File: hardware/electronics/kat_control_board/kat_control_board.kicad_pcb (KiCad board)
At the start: 4 copper layers, 84.2 x 173.5 mm, 122 parts, among them J1 USB_C_Receptacle_USB2.0, J10 Conn_01x04, J11 Conn_01x04, J12 Conn_01x04, J13 Conn_01x04, J14 Conn_01x04, J15 Conn_01x04, J16 Conn_01x04, J17 Conn_01x02, J18 Conn_01x04, J19 Conn_01x04, J2 Conn_01x04, J20 Conn_01x02, J21 Conn_01x02, J22 Conn_01x02, J23 Conn_01x02, J24 Conn_01x02, J25 Conn_01x02, J26 Conn_01x02, J27 Conn_01x02, J28 Conn_01x04, J29 Conn_02x30_Odd_Even, J3 Conn_01x04, J30 Conn_02x30_Odd_Even, J31 Conn_02x30_Odd_Even, J32 Conn_02x30_Odd_Even, J4 Conn_01x04, J5 Conn_01x04, J6 Conn_01x04, J7 Conn_01x04, J8 Conn_01x04, J9 Conn_01x04, Q1 AO3400A, Q2 AO3400A, Q3 AO3400A, Q4 AO3400A, Q5 AO3400A, SW1 SW_SPST, SW2 SW_SPST, U1 RP2040, U2 W25Q128JVS, U3 SN74HC4851, U4 74HCT244, U5 74HCT244, U6 SIC431, U7 XC6206PxxxMR, Y1 12MHz

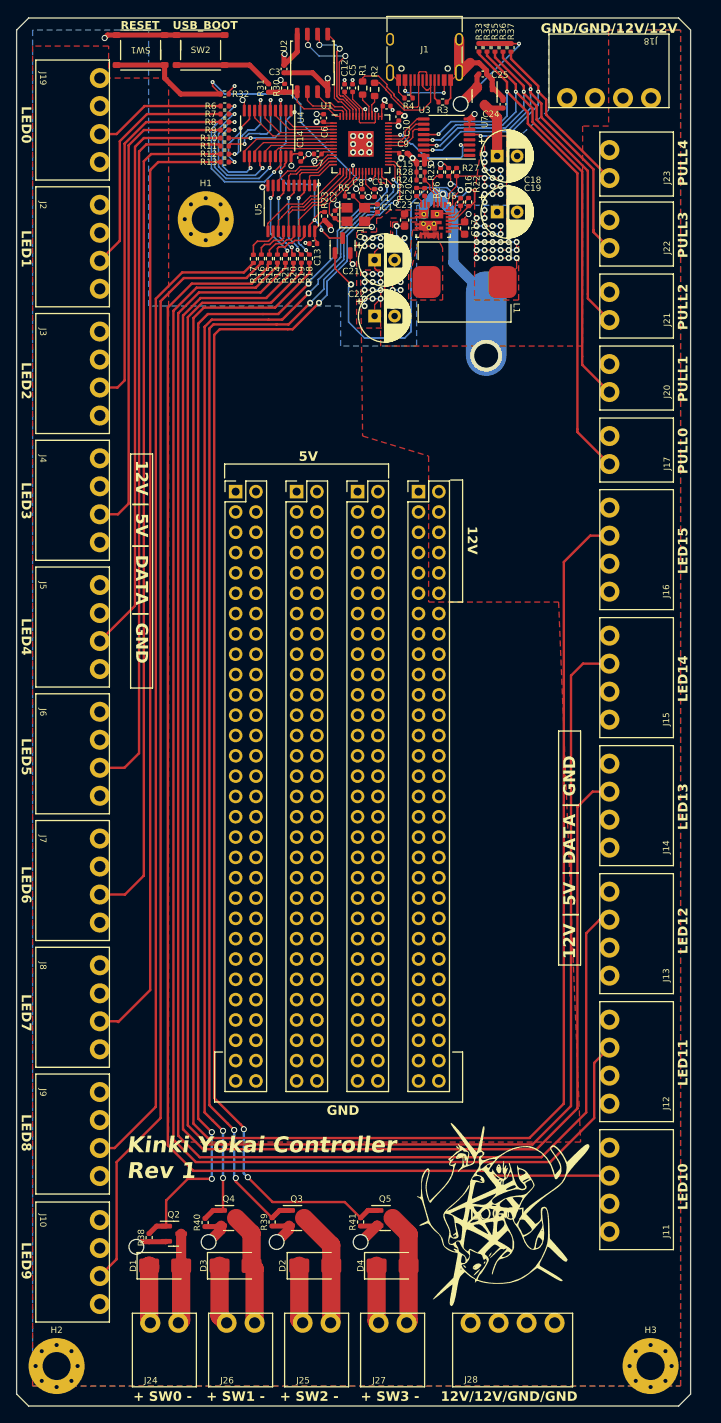
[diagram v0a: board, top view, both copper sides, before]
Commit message: Updated PCB design with more protections
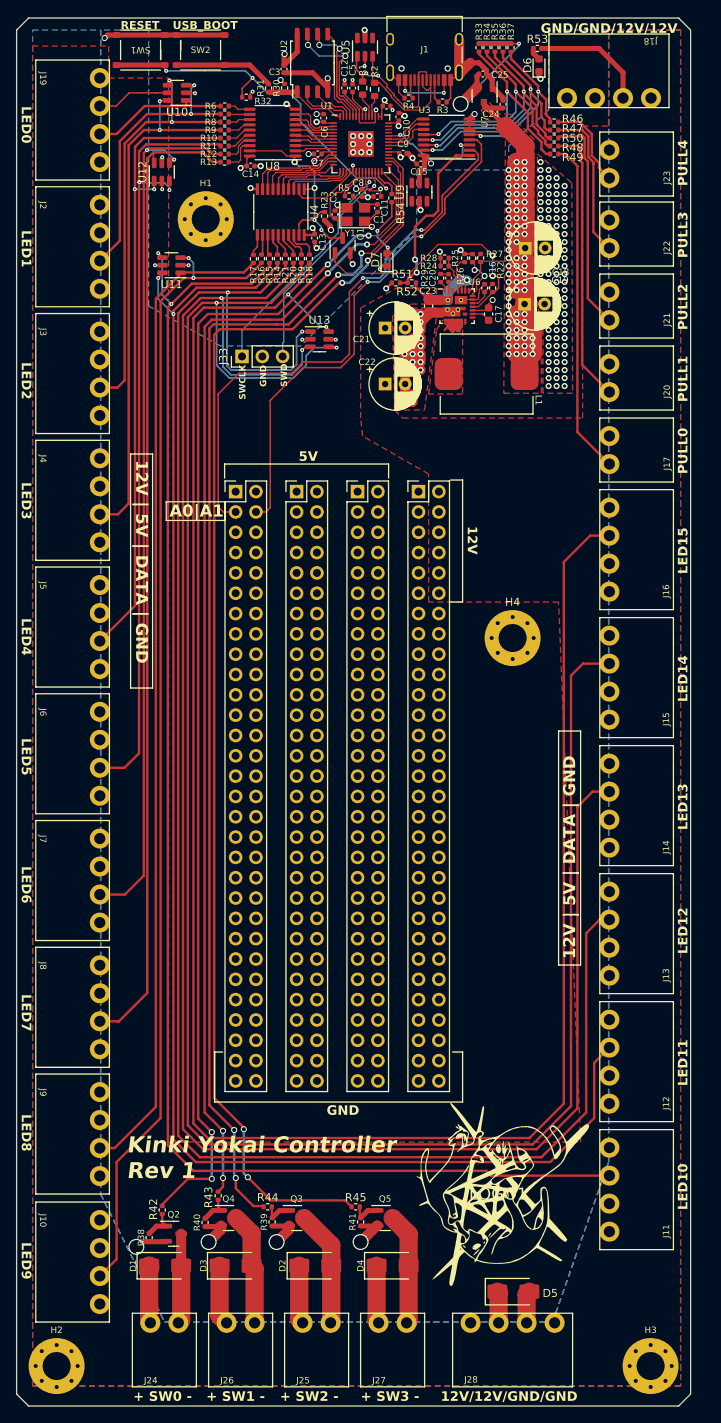
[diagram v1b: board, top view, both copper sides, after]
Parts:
- added D5: M7, Diode_SMD:D_SMA, F.Cu at (90.6, 176.2)
- added D6: RED, LED_SMD:LED_0603_1608Metric, F.Cu at (93.8, 22.9)
- added D7: YELLOW, LED_SMD:LED_0603_1608Metric, F.Cu at (74.8, 47.2)
- added H4: MountingHole, MountingHole:MountingHole_3.5mm_Pad_Via, F.Cu at (90.5, 94.5)
- added J33: Conn_01x03, Connector_PinHeader_2.54mm:PinHeader_1x03_P2.54mm_Vertical, F.Cu at (56.7, 59.3)
- added R42: 100R, Resistor_SMD:R_0402_1005Metric, F.Cu at (46.7, 166.0)
- added R43: 100R, Resistor_SMD:R_0402_1005Metric, F.Cu at (53.7, 164.2)
- added R44: 100R, Resistor_SMD:R_0402_1005Metric, F.Cu at (59.9, 165.6)
- added R45: 100R, Resistor_SMD:R_0402_1005Metric, F.Cu at (70.9, 165.6)
- added R46: 100R, Resistor_SMD:R_0402_1005Metric, F.Cu at (95.7, 30.0)
- added R47: 100R, Resistor_SMD:R_0402_1005Metric, F.Cu at (95.7, 31.0)
- added R48: 100R, Resistor_SMD:R_0402_1005Metric, F.Cu at (95.7, 33.0)
- added R49: 100R, Resistor_SMD:R_0402_1005Metric, F.Cu at (95.7, 34.0)
- added R50: 100R, Resistor_SMD:R_0402_1005Metric, F.Cu at (95.7, 32.0)
- added R51: 1kR, Resistor_SMD:R_0402_1005Metric, F.Cu at (75.9, 50.1)
- added R52: 7.5kR, Resistor_SMD:R_0402_1005Metric, F.Cu at (77.9, 50.1)
- added R53: 1kR, Resistor_SMD:R_0402_1005Metric, F.Cu at (93.6, 20.8)
- added R54: 330R, Resistor_SMD:R_0402_1005Metric, F.Cu at (75.4, 39.5)
- added U10: SRV05-4, Package_TO_SOT_SMD:SOT-23-6, F.Cu at (48.6, 26.4)
- added U11: SRV05-4, Package_TO_SOT_SMD:SOT-23-6, F.Cu at (47.9, 47.9)
- added U12: SRV05-4, Package_TO_SOT_SMD:SOT-23-6, F.Cu at (46.6, 36.2)
- added U13: SRV05-4, Package_TO_SOT_SMD:SOT-23-6, F.Cu at (66.4, 57.1)
- added U8: 74HCT541, Package_SO:TSSOP-20_4.4x6.5mm_P0.65mm, F.Cu at (60.5, 31.3)
- added U9: SRV05-4, Package_TO_SOT_SMD:SOT-23-6, F.Cu at (78.8, 38.8)
- U4: value 74HCT244 -> 74HCT541
- U5: value 74HCT244 -> SRV05-4; footprint Package_SO:TSSOP-20_4.4x6.5mm_P0.65mm -> Package_TO_SOT_SMD:SOT-23-6
- moved U5 22.2 mm to (72.0, 20.6), turned to 90 degrees
- moved C18 12.0 mm to (92.1, 45.8)
- moved C19 12.0 mm to (92.0, 52.8)
- moved L1 11.8 mm to (87.2, 61.5)
- moved C16 11.2 mm to (87.0, 50.8)
- moved C17 11.2 mm to (87.5, 54.0)
- moved C20 11.2 mm to (82.5, 49.5)
- moved C23 11.2 mm to (80.0, 53.0)
- moved R22 11.2 mm to (88.0, 50.8)
- moved R24 11.2 mm to (82.0, 48.0)
- moved R25 11.2 mm to (84.5, 47.0)
- moved R26 11.2 mm to (85.5, 47.0)
- moved R27 11.2 mm to (86.5, 47.0)
- moved R28 11.2 mm to (82.0, 47.0)
- moved R29 11.2 mm to (81.5, 49.5)
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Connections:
- J17 pad 1: /PULL0 -> Net-(J17-Pin_1)
- J20 pad 1: /PULL1 -> Net-(J20-Pin_1)
- J21 pad 1: /PULL2 -> Net-(J21-Pin_1)
- J22 pad 1: /PULL3 -> Net-(J22-Pin_1)
- J23 pad 1: /PULL4 -> Net-(J23-Pin_1)
- J29 pad 3: unconnected-(J29-Pin_3-Pad3) -> /A0
- J29 pad 4: unconnected-(J29-Pin_4-Pad4) -> /A1
- Q2 pad 1: /SW0 -> Net-(Q2-G)
- Q3 pad 1: /SW2 -> Net-(Q3-G)
- Q4 pad 1: /SW1 -> Net-(Q4-G)
- Q5 pad 1: /SW3 -> Net-(Q5-G)
- R10 pad 1: Net-(U4-2Y0) -> Net-(U8-Y3)
- R11 pad 1: Net-(U4-2Y1) -> Net-(U8-Y2)
- R12 pad 1: Net-(U4-2Y2) -> Net-(U8-Y1)
- R13 pad 1: Net-(U4-2Y3) -> Net-(U8-Y0)
- R14 pad 1: Net-(U5-1Y0) -> Net-(U4-Y4)
- R15 pad 1: Net-(U5-1Y1) -> Net-(U4-Y5)
- R16 pad 1: Net-(U5-1Y2) -> Net-(U4-Y6)
- R17 pad 1: Net-(U5-1Y3) -> Net-(U4-Y7)
- R18 pad 1: Net-(U5-2Y0) -> Net-(U4-Y0)
- R19 pad 1: Net-(U5-2Y1) -> Net-(U4-Y1)
- R20 pad 1: Net-(U5-2Y2) -> Net-(U4-Y2)
- R21 pad 1: Net-(U5-2Y3) -> Net-(U4-Y3)
- R38 pad 1: /SW0 -> Net-(Q2-G)
- R39 pad 1: /SW2 -> Net-(Q3-G)
- R40 pad 1: /SW1 -> Net-(Q4-G)
- R41 pad 1: /SW3 -> Net-(Q5-G)
- R6 pad 1: Net-(U4-1Y0) -> Net-(U8-Y7)
- R7 pad 1: Net-(U4-1Y1) -> Net-(U8-Y6)
- R8 pad 1: Net-(U4-1Y2) -> Net-(U8-Y5)
- R9 pad 1: Net-(U4-1Y3) -> Net-(U8-Y4)
- U1 pad 11: Net-(U1-GPIO8) -> /LED8_IN
- U1 pad 12: Net-(U1-GPIO9) -> /LED9_IN
- U1 pad 13: Net-(U1-GPIO10) -> /LED10_IN
- U1 pad 14: Net-(U1-GPIO11) -> /LED11_IN
- U1 pad 15: Net-(U1-GPIO12) -> /LED12_IN
- U1 pad 16: Net-(U1-GPIO13) -> /LED13_IN
- U1 pad 17: Net-(U1-GPIO14) -> /LED14_IN
- U1 pad 18: Net-(U1-GPIO15) -> /LED15_IN
- U1 pad 2: Net-(U1-GPIO0) -> /LED0_IN
- U1 pad 24: unconnected-(U1-SWCLK-Pad24) -> Net-(J33-Pin_1)
- U1 pad 25: unconnected-(U1-SWD-Pad25) -> Net-(J33-Pin_3)
- U1 pad 27: /SW0 -> /STATUS_LED
- U1 pad 28: /SW1 -> /SW0
- U1 pad 29: /SW2 -> /SW1
- U1 pad 3: Net-(U1-GPIO1) -> /LED1_IN
- U1 pad 30: /SW3 -> /SW2
- U1 pad 31: unconnected-(U1-GPIO20-Pad31) -> /SW3
- U1 pad 4: Net-(U1-GPIO2) -> /LED2_IN
- U1 pad 5: Net-(U1-GPIO3) -> /LED3_IN
- U1 pad 6: Net-(U1-GPIO4) -> /LED4_IN
- U1 pad 7: Net-(U1-GPIO5) -> /LED5_IN
- U1 pad 8: Net-(U1-GPIO6) -> /LED6_IN
- U1 pad 9: Net-(U1-GPIO7) -> /LED7_IN
- U3 pad 1: unconnected-(U3-X4-Pad1) -> /12V_SENSE
- U3 pad 2: unconnected-(U3-X6-Pad2) -> /A0
- U3 pad 4: unconnected-(U3-X7-Pad4) -> /A1
- U4 pad 11: Net-(U1-GPIO4) -> Net-(U4-Y7)
- U4 pad 12: Net-(U4-1Y3) -> Net-(U4-Y6)
- U4 pad 13: Net-(U1-GPIO5) -> Net-(U4-Y5)
- U4 pad 14: Net-(U4-1Y2) -> Net-(U4-Y4)
- U4 pad 15: Net-(U1-GPIO6) -> Net-(U4-Y3)
- U4 pad 16: Net-(U4-1Y1) -> Net-(U4-Y2)
- U4 pad 17: Net-(U1-GPIO7) -> Net-(U4-Y1)
- U4 pad 18: Net-(U4-1Y0) -> Net-(U4-Y0)
- U4 pad 2: Net-(U1-GPIO0) -> /LED15_IN
- U4 pad 3: Net-(U4-2Y0) -> /LED14_IN
- U4 pad 4: Net-(U1-GPIO1) -> /LED13_IN
- U4 pad 5: Net-(U4-2Y1) -> /LED12_IN
- U4 pad 6: Net-(U1-GPIO2) -> /LED11_IN
- U4 pad 7: Net-(U4-2Y2) -> /LED10_IN
- U4 pad 8: Net-(U1-GPIO3) -> /LED9_IN
- U4 pad 9: Net-(U4-2Y3) -> /LED8_IN
- U5 pad 1: /~{LED_PWR} -> /USB_DP
- U5 pad 2: Net-(U1-GPIO11) -> GND
- U5 pad 3: Net-(U5-2Y0) -> /USB_DM
- U5 pad 4: Net-(U1-GPIO10) -> unconnected-(U5-IO3-Pad4)
- U5 pad 5: Net-(U5-2Y1) -> +3V3
- U5 pad 6: Net-(U1-GPIO9) -> unconnected-(U5-IO4-Pad6)
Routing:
- net /A0: track 0.00 -> 70.0 mm, vias 0 -> 2
- net /A1: track 0.00 -> 64.3 mm, vias 0 -> 2
- net Net-(J17-Pin_1): track 0.00 -> 41.9 mm
- net /PULL0: track 72.9 -> 31.3 mm
- net Net-(J20-Pin_1): track 0.00 -> 34.8 mm
- net /PULL1: track 64.4 -> 30.8 mm
- net Net-(J33-Pin_1): track 0.00 -> 29.8 mm, vias 0 -> 1
- net Net-(J33-Pin_3): track 0.00 -> 28.4 mm, vias 0 -> 1
- net Net-(J21-Pin_1): track 0.00 -> 27.5 mm
- net /LED14: track 228.8 -> 255.6 mm, vias 0 -> 2
- net /PULL2: track 56.1 -> 30.5 mm
- net /LED12: track 199.6 -> 223.5 mm, vias 0 -> 2
- net +12V: track 83.3 -> 59.9 mm, vias 21 -> 1
- net /LED13: track 213.8 -> 236.3 mm, vias 0 -> 2
- net /12V_SENSE: track 0.00 -> 22.0 mm, vias 0 -> 2
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- added copper zone on B.Cu, net +12V
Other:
- board text added: "A0|A1"
- board text added: "SWCLK"
- board text added: "SWD"
